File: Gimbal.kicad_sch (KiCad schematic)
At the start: 8 parts, among them U1 ESP32-WROOM-32U, U2 BMI088

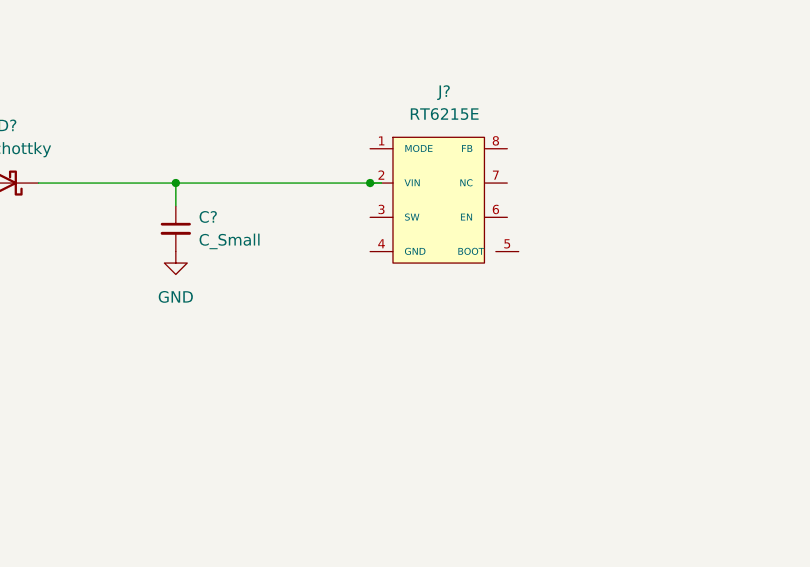
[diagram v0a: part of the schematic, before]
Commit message: fixed boot pin
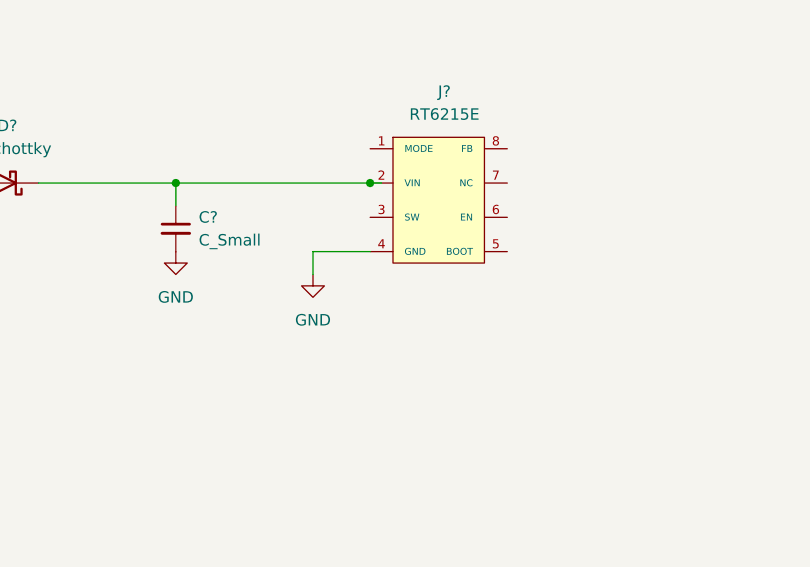
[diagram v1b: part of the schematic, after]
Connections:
- net GND: now also J?.4 (GND)
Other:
- moved on the sheet: J?
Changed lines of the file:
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@@
+    (stroke (width 0) (type default) (color 0 0 0 0))
+  )
+  (wire (pts (xy 104.14 207.01) (xy 104.14 209.55))
     (stroke (width 0) (type default) (color 0 0 0 0))
   )
@@
   )
   (wire (pts (xy 48.26 199.39) (xy 66.04 199.39))
+    (stroke (width 0) (type default) (color 0 0 0 0))
+  )
+  (wire (pts (xy 110.49 207.01) (xy 104.14 207.01))
     (stroke (width 0) (type default) (color 0 0 0 0))
   )
@@
     (pin "2")
   )
+  (symbol (lib_id "power:GND") (at 104.14 209.55 0) (unit 1)
+    (in_bom yes) (on_board yes) (fields_autoplaced)
+    (property "Reference" "#PWR?" (id 0) (at 104.14 215.9 0)
+      (effects (font (size 1.27 1.27)) hide)
+    )
+    (property "Value" "GND" (id 1) (at 104.14 214.63 0))
+    (property "Footprint" "" (id 2) (at 104.14 209.55 0)
+      (effects (font (size 1.27 1.27)) hide)
+    )
+    (property "Datasheet" "" (id 3) (at 104.14 209.55 0)
+      (effects (font (size 1.27 1.27)) hide)
+    )
+    (pin "1")
+  )
   (symbol (lib_id "Device:C_Small") (at 417.83 199.39 0) (unit 1)
     (in_bom yes) (on_board yes) (fields_autoplaced)
@@
       (reference "#PWR?") (unit 1) (value "+3V3") (footprint "")
     )
+    (path "/7ec59656-26ad-4f79-8ec2-8d25250f200c"
+      (reference "#PWR?") (unit 1) (value "GND") (footprint "")
+    )
     (path "/b128eade-3261-4888-803b-49d9962a48be"

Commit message: finished erc check
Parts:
- removed C?: C_Small, symbol Device:C_Small
- removed J?: RT6215E, symbol GIMBAL:RT6215E
- added C1, C11, C6: 22uF, symbol Device:C_Small
- added C2, C5, C8: 0.1uF, symbol Device:C_Small
- added C3: 1uF, symbol Device:C_Small
- added C4, C7: 10uF, symbol Device:C_Small
- added D2, D3, D4: DIODE, symbol Simulation_SPICE:DIODE
- added D5: LED, symbol Device:LED
- added J2: USB_C_Receptacle_USB2.0, symbol Connector:USB_C_Receptacle_USB2.0
- added J3, J4, J5: 0022232041, digikey-footprints:PinHeader_1x4_P2.54mm_Drill1.02mm, symbol dk_Rectangular-Connectors-Headers-Male-Pins:0022232041
- added J6: Conn_01x02, symbol Connector_Generic:Conn_01x02
- added Q1, Q2: Q_NPN_BCE, symbol Device:Q_NPN_BCE
- added R1, R4: 100, symbol Device:R_US
- added R10, R7, R8, R9: 500m, symbol Device:R_US
- added R2: 22.1k, symbol Device:R_US
- added R3: 47.5k, symbol Device:R_US
- added R5, R6: 10k, symbol Device:R_US
- added SW1: SW_Push, symbol Switch:SW_Push
- added U3: CP2102N-Axx-xQFN28, Package_DFN_QFN:QFN-28-1EP_5x5mm_P0.5mm_EP3.35x3.35mm, symbol Interface_USB:CP2102N-Axx-xQFN28
- added U4: TLV70433DBVT, symbol GIMBAL:TLV70433DBVT
- added U5, U6: DRV8846RGET, symbol GIMBAL:DRV8846RGET
- gave numbers to parts that had none: 4
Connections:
- net +3V3: now also C3.1, J5.3, R4.1, U3.6 (VDD), U4.1 (OUT)
- net GND: now also C1.2, C11.2, C2.1, C3.2, C4.2, C5.2, C6.2, C7.2, C8.2, D2.1 (A), D3.1 (A), D4.1 (A), D5.1 (K), J2.A1 (GND), J2.A12 (GND), J2.B1 (GND), J2.B12 (GND), J5.1, R1.2, R10.2, R3.2, R7.2, R8.2, R9.2, SW1.2, U3.29 (GND), U3.3 (GND), U4.2 (GND), U5.11 (nENBL), U5.18 (GND), U6.11 (nENBL), U6.18 (GND)
- net ESPIO25: now reaches U1.10 (IO25)
- net ESPIO25: now also U2.16 (INT1)
- net ESPIO26: now reaches U1.11 (IO26)
- net ESPIO26: now also U2.12 (INT3)
- net SPI_CLK: now reaches U1.13 (IO14)
- net SPI_CLK: now also U2.8 (SCK)
- net SPI_MISO: now reaches U1.14 (IO12)
- net SPI_MISO: now also U2.10 (SDO2), U2.15 (SDO1)
- net SPI_MOSI: now reaches U1.16 (IO13)
- net SPI_MOSI: now also U2.9 (SDI)
- net Motor1M1: now reaches U1.23 (IO15)
- net Motor1M1: now also U5.9 (M1)
- net ESPIO0: now reaches U1.25 (IO0)
- net ESPIO0: now also Q1.2 (C)
- net Motor1M0: now reaches U1.27 (IO16)
- net Motor1M0: now also U5.8 (M0)
- net Motor1Dir: now reaches U1.28 (IO17)
- net Motor1Dir: now also U5.13 (DIR)
- net EN: now reaches U1.3 (EN)
- net EN: now also C2.2, Q2.2 (C), SW1.1
- net Motor1Step: now reaches U1.30 (IO18)
- net Motor1Step: now also U5.12 (STEP)
- net Motor2M1: now reaches U1.31 (IO19)
- net Motor2M1: now also U6.9 (M1)
- net Motor2M0: now reaches U1.33 (IO21)
- net Motor2M0: now also U6.8 (M0)
- net RX: now reaches U1.34 (RXD0/IO3)
- net RX: now also J6.2 (Pin_2), U3.25 (RXD)
- net TX: now reaches U1.35 (TXD0/IO1)
- net TX: now also J6.1 (Pin_1), U3.26 (TXD)
- net Motor2Dir: now reaches U1.36 (IO22)
- net Motor2Dir: now also U6.13 (DIR)
- net Motor2Step: now reaches U1.37 (IO23)
- net Motor2Step: now also U6.12 (STEP)
- net ESPIO32: now reaches U1.8 (IO32)
- net ESPIO32: now also U2.14 (CSB1)
- net ESPIO33: now reaches U1.9 (IO33)
- net ESPIO33: now also U2.5 (CSB2)
- net +12V: now reaches D1.1 (K)
- net +12V: now also C1.1, C4.1, C5.1, C7.1, C8.1, J5.2, U4.3 (IN), U5.15 (VM), U6.15 (VM)
- new net: Q1.1 (B), R5.2
- new net: C6.1, U5.14 (VREF), U5.17 (VINT)
- new net: R7.1, U5.2 (AISEN)
- new net: R8.1, U5.5 (BISEN)
- new net: Q2.1 (B), R6.2
- new net: R2.2, R3.1, U3.8 (VBUS)
- new net: D4.2 (K), J2.A6 (D+), J2.B6 (D+), U3.4 (D+)
- new net: D3.2 (K), J2.A7 (D-), J2.B7 (D-), U3.5 (D-)
- new net: D5.2 (A), R4.2
- new net: C11.1, U6.14 (VREF), U6.17 (VINT)
- new net: R10.1, U6.5 (BISEN)
- new net: J2.S1 (SHIELD), R1.1
- new net: R9.1, U6.2 (AISEN)
- new net !DTR: Q1.3 (E), R6.1, U3.28 (~{DTR})
- new net !RTS: Q2.3 (E), R5.1, U3.24 (~{RTS})
- new net Motor1Out1: J3.1, U5.1 (AOUT1)
- new net Motor1Out2: J3.2, U5.3 (AOUT2)
- new net Motor1Out3: J3.3, U5.6 (BOUT1)
- new net Motor1Out4: J3.4, U5.4 (BOUT2)
- new net Motor2Out1: J4.1, U6.1 (AOUT1)
- new net Motor2Out2: J4.2, U6.3 (AOUT2)
- new net Motor2Out3: J4.3, U6.6 (BOUT1)
- new net Motor2Out4: J4.4, U6.4 (BOUT2)
- new net VBUS: D2.2 (K), J2.A4 (VBUS), J2.A9 (VBUS), J2.B4 (VBUS), J2.B9 (VBUS), R2.1, U3.7 (VREGIN), U3.9 (~{RST})
- no-connect marks 1 -> 54
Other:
- note added: "BREAKOUTS"
- note added: "ESP"
- note added: "IMU"
- note added: "MOTOR"
- note added: "MOTOR DRIVER"
- note added: "POWER"
- moved on the sheet: C10, C9, D1, J1, U1, U2
